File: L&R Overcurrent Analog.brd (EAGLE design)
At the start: 100 x 80 mm, 17 parts, among them IC1 CSLA2CFTH, IC2 TLC393CPN, Q1 SUP75P0307, Q2 SUP75P0307, X1 J1

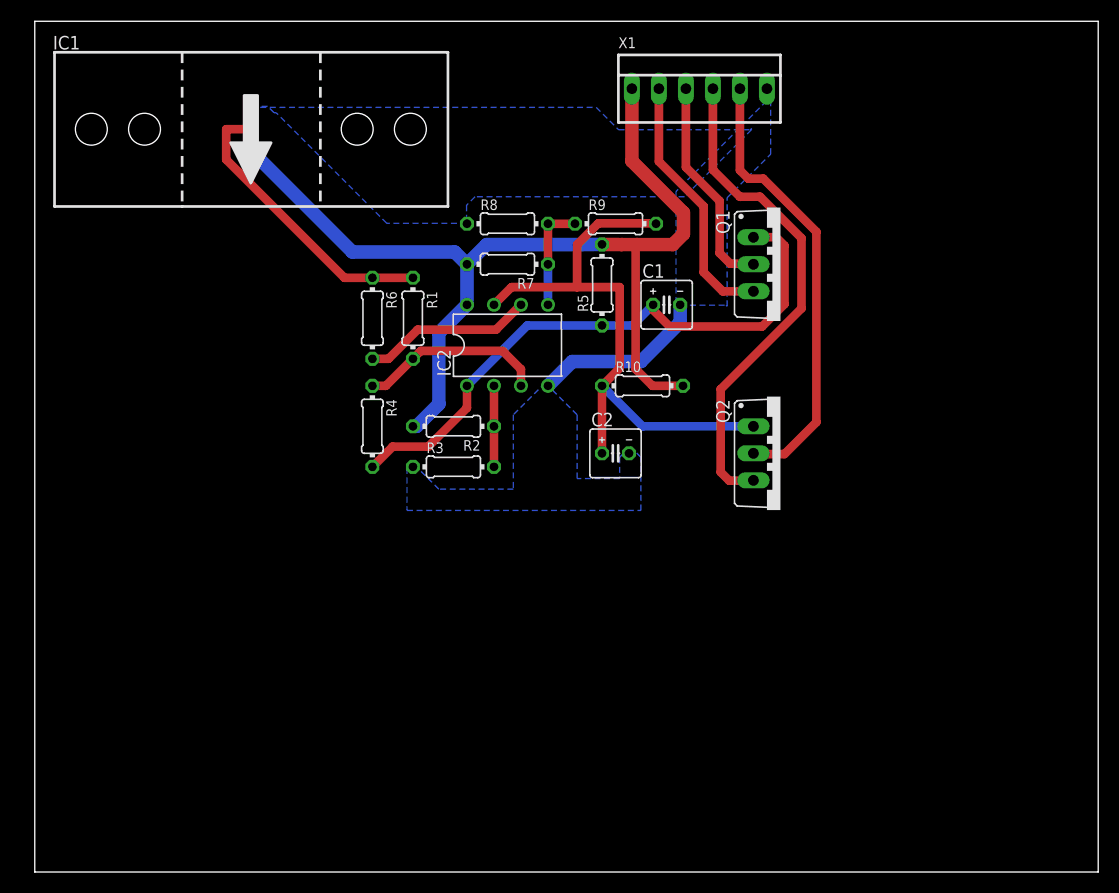
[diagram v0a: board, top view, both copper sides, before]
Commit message: Moved current transducer closer on board, larger ground pour.
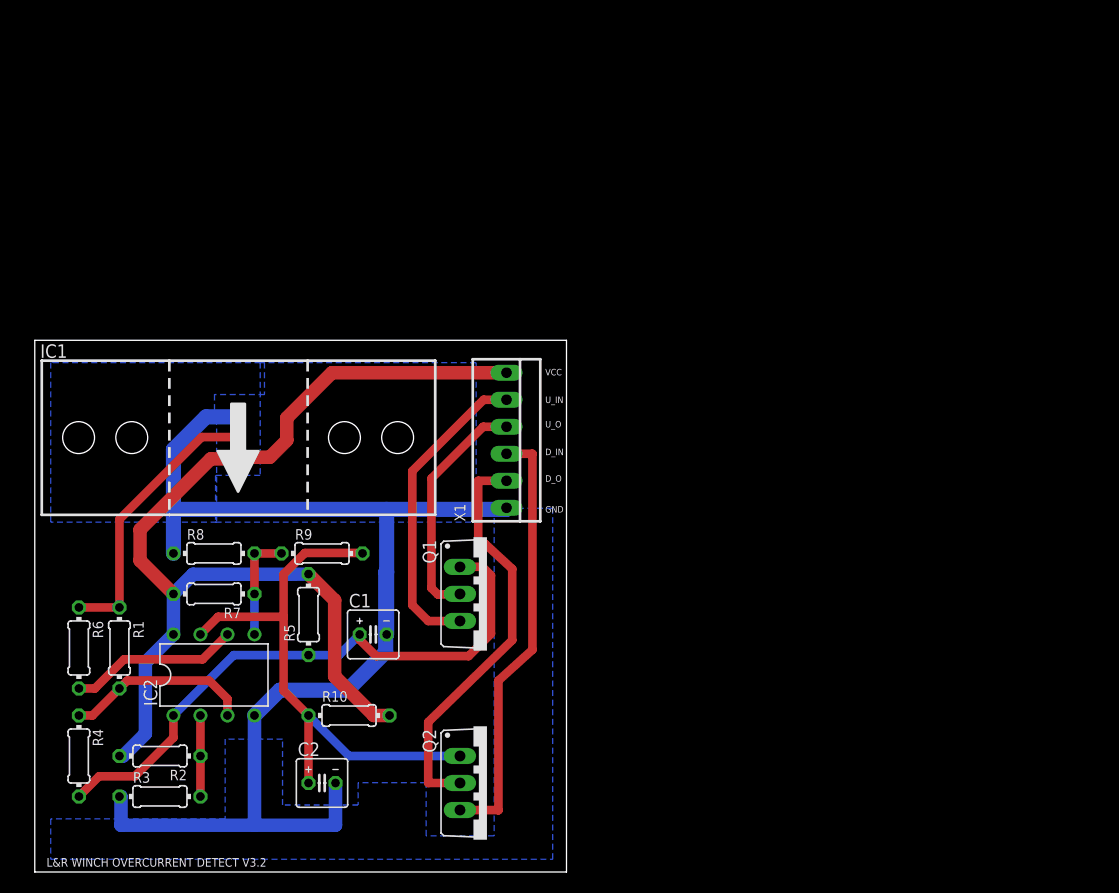
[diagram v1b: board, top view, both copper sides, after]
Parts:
- moved C1 41.5 mm to (31.8, 22.3)
- moved C2 41.5 mm to (27.0, 8.37)
- moved IC2 41.5 mm to (16.9, 18.5)
- moved Q1 41.5 mm to (42.5, 26.1)
- moved Q2 41.5 mm to (42.5, 8.37)
- moved R1 41.5 mm to (7.96, 21.1)
- moved R10 41.5 mm to (29.6, 14.7)
- moved R3 41.5 mm to (11.8, 7.10)
- moved R5 41.5 mm to (25.7, 24.2)
- moved R6 41.5 mm to (4.15, 21.1)
- moved R7 41.5 mm to (16.9, 26.1)
- moved R8 41.5 mm to (16.9, 30.0)
- moved R9 41.5 mm to (27.0, 30.0)
- moved R2 41.5 mm to (11.8, 10.9)
- moved R4 41.5 mm to (4.15, 10.9)
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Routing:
- net GND: track 16.6 -> 120.1 mm
- net N$10: track 47.2 -> 41.0 mm
- net N$8: track 24.4 -> 29.3 mm
- net N$7: track 57.0 -> 53.3 mm
- net N$11: track 42.3 -> 39.1 mm
- net N$9: track 20.4 -> 22.3 mm
- net +12V: track 96.4 -> 97.5 mm
- net N$3: track 27.3 -> 26.5 mm
- removed copper zone on layer 16, net N$12
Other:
- board size 100 x 80 mm -> 50 x 50 mm
- board text added: "D_IN"
- board text added: "D_O"
- board text added: "GND"
- board text added: "L&R WINCH OVERCURRENT DETECT V3.2"
- board text added: "U_IN"
- board text added: "U_O"
- board text added: "VCC"

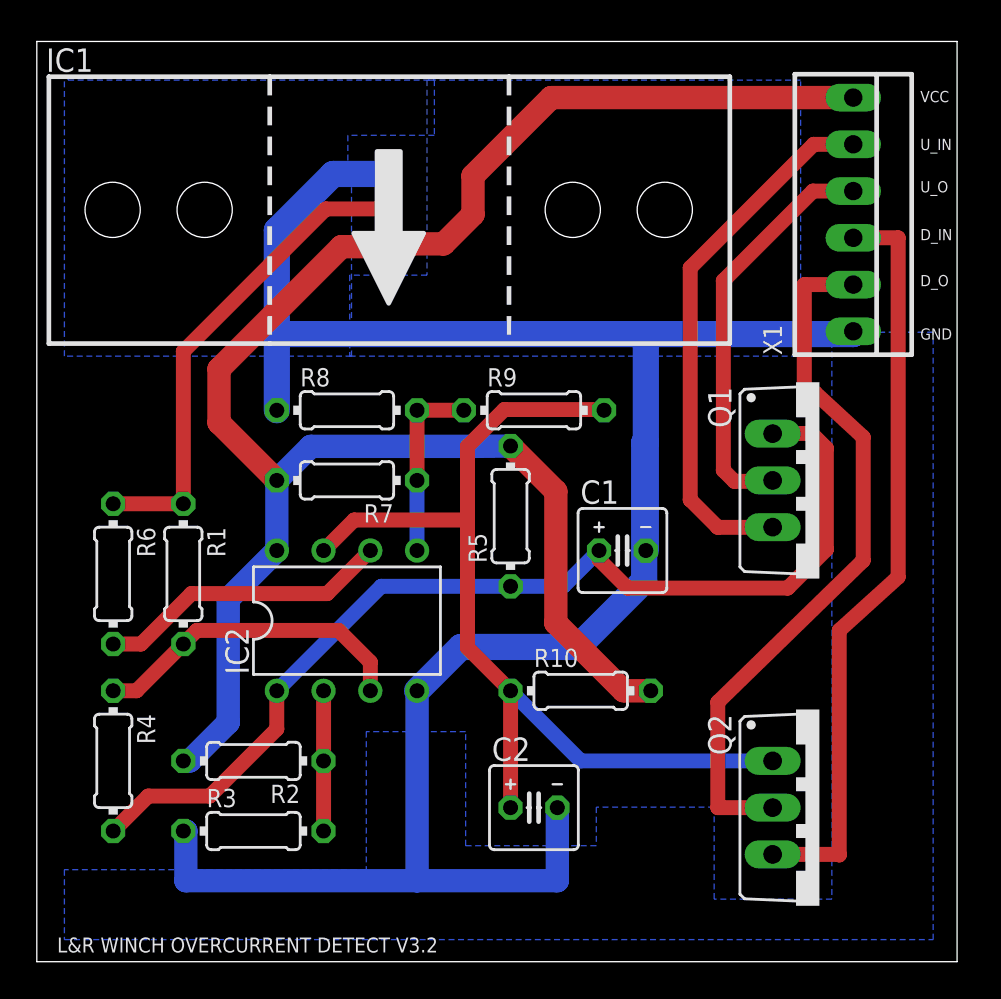
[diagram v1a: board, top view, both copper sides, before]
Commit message: Added IC filter cap, changed RC timer caps to electrolytic.
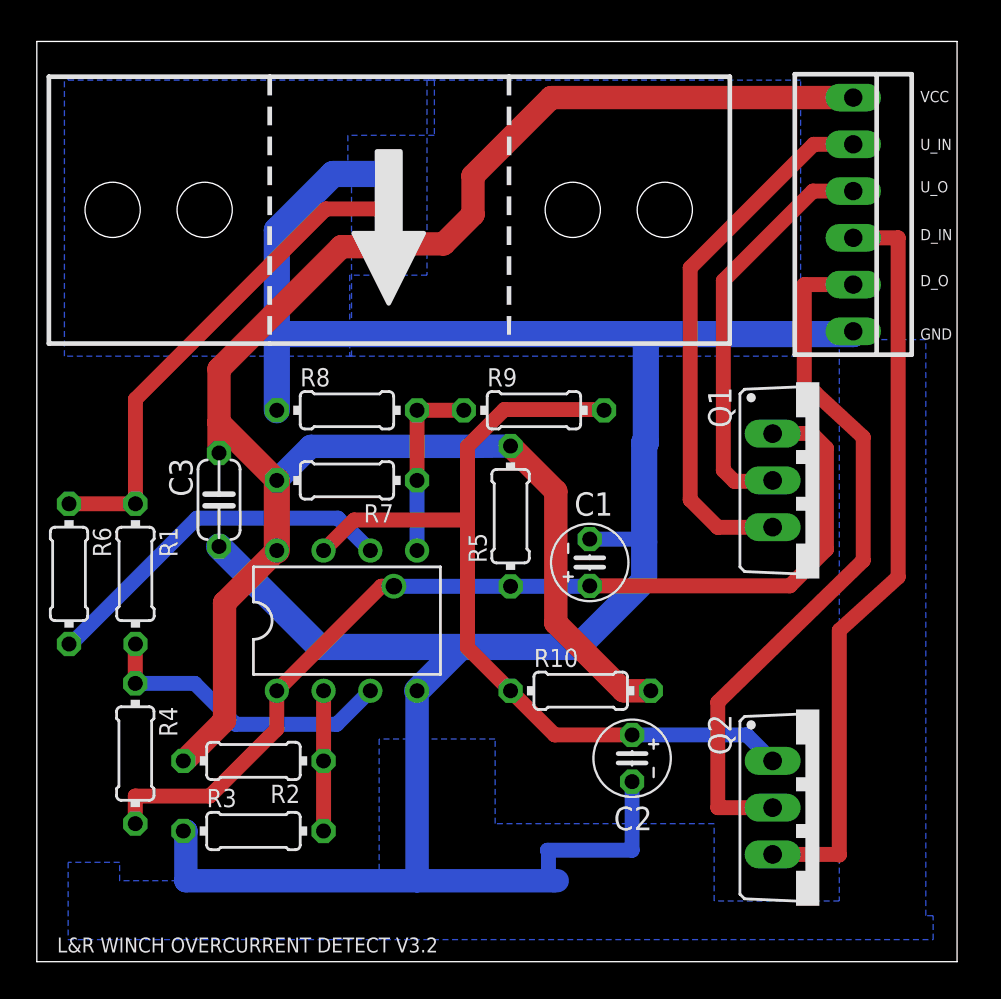
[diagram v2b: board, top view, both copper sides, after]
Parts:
- added C3: 0.1u, Overcurrent Detect:C050-024X044
- moved C2 5.97 mm to (32.3, 11.1), turned to 270 degrees
- moved R1 2.60 mm to (5.36, 21.1)
- moved R6 2.40 mm to (1.75, 21.1)
- moved C1 1.89 mm to (30.0, 21.7), turned to 90 degrees
- moved R4 1.26 mm to (5.35, 11.3)
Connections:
- net +12V: now also C3.1
- net GND: now also C3.2
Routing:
- net GND: track 120.1 -> 138.8 mm
- net N$7: track 53.3 -> 46.9 mm
- net N$4: track 16.1 -> 19.9 mm
- net N$6: track 57.0 -> 54.6 mm, vias 0 -> 1
- net +12V: track 97.5 -> 99.0 mm
- net N$1: track 17.6 -> 16.6 mm
- net N$3: track 26.5 -> 27.4 mm

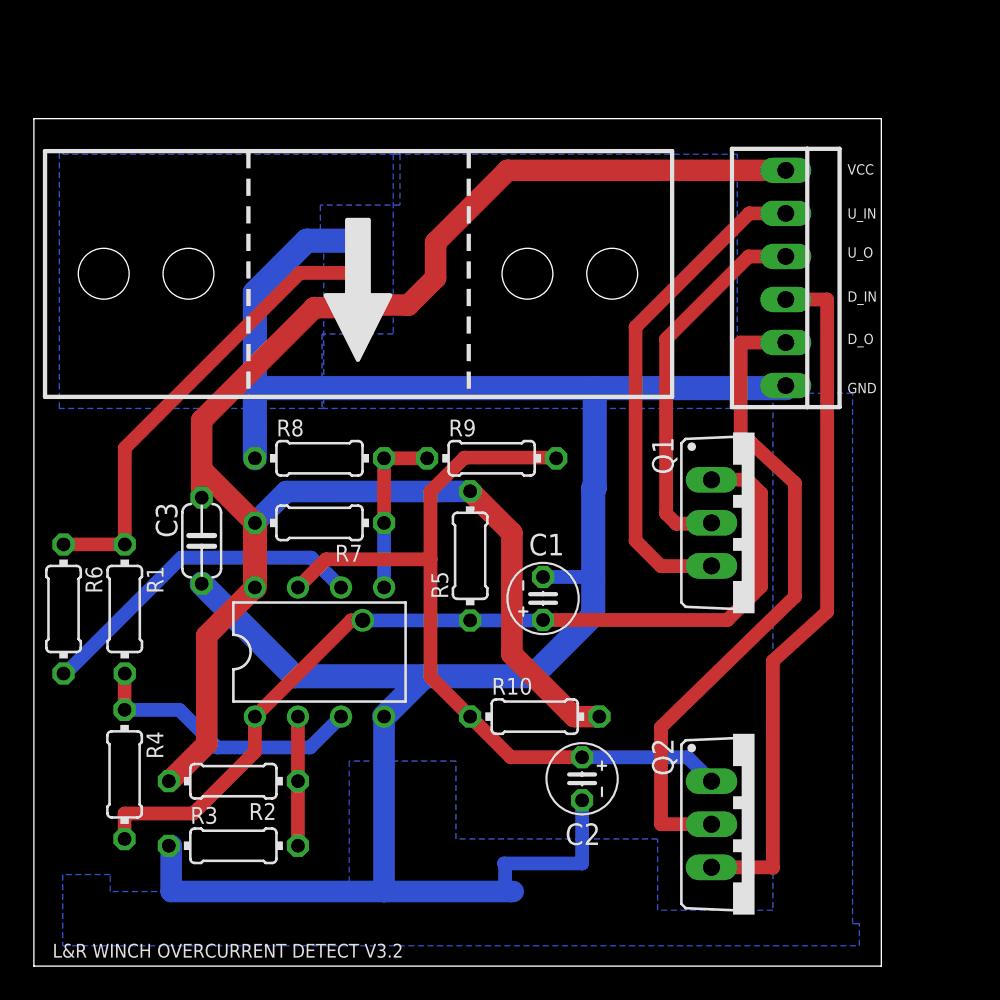
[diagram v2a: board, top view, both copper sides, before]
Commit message: Added stand off holes to board, increased board size.
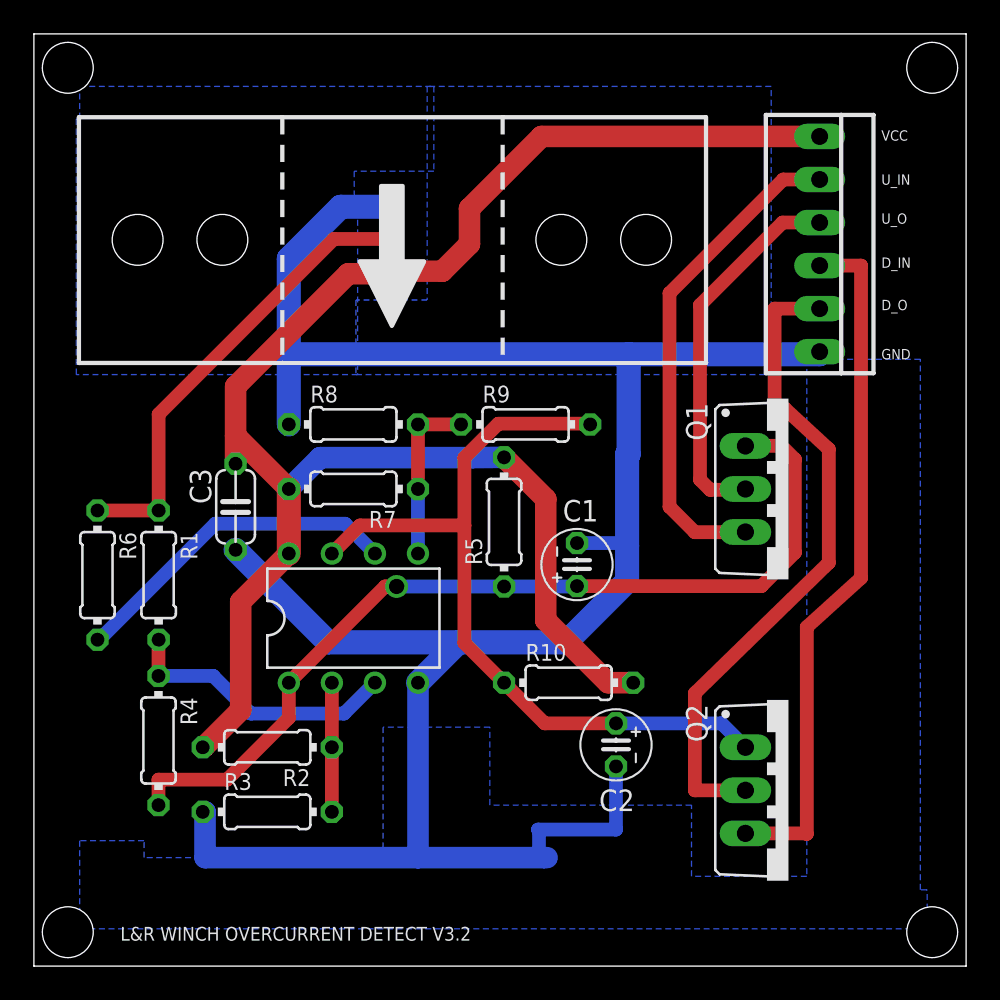
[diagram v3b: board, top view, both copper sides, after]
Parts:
- moved C1 2.83 mm to (32.0, 23.7)
- moved C2 2.83 mm to (34.3, 13.1)
- moved C3 2.83 mm to (11.9, 27.1)
- moved IC1 2.83 mm to (21.1, 42.9)
- moved IC2 2.83 mm to (18.9, 20.5)
- moved Q1 2.83 mm to (44.5, 28.1)
- moved Q2 2.83 mm to (44.5, 10.4)
- moved R1 2.83 mm to (7.36, 23.1)
- moved R2 2.83 mm to (13.8, 12.9)
- moved R3 2.83 mm to (13.8, 9.10)
- moved R4 2.83 mm to (7.35, 13.3)
- moved R5 2.83 mm to (27.7, 26.2)
- moved R6 2.83 mm to (3.75, 23.1)
- moved R7 2.83 mm to (18.9, 28.1)
- moved R8 2.83 mm to (18.9, 32.0)
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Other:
- board size 50 x 50 mm -> 55 x 55 mm

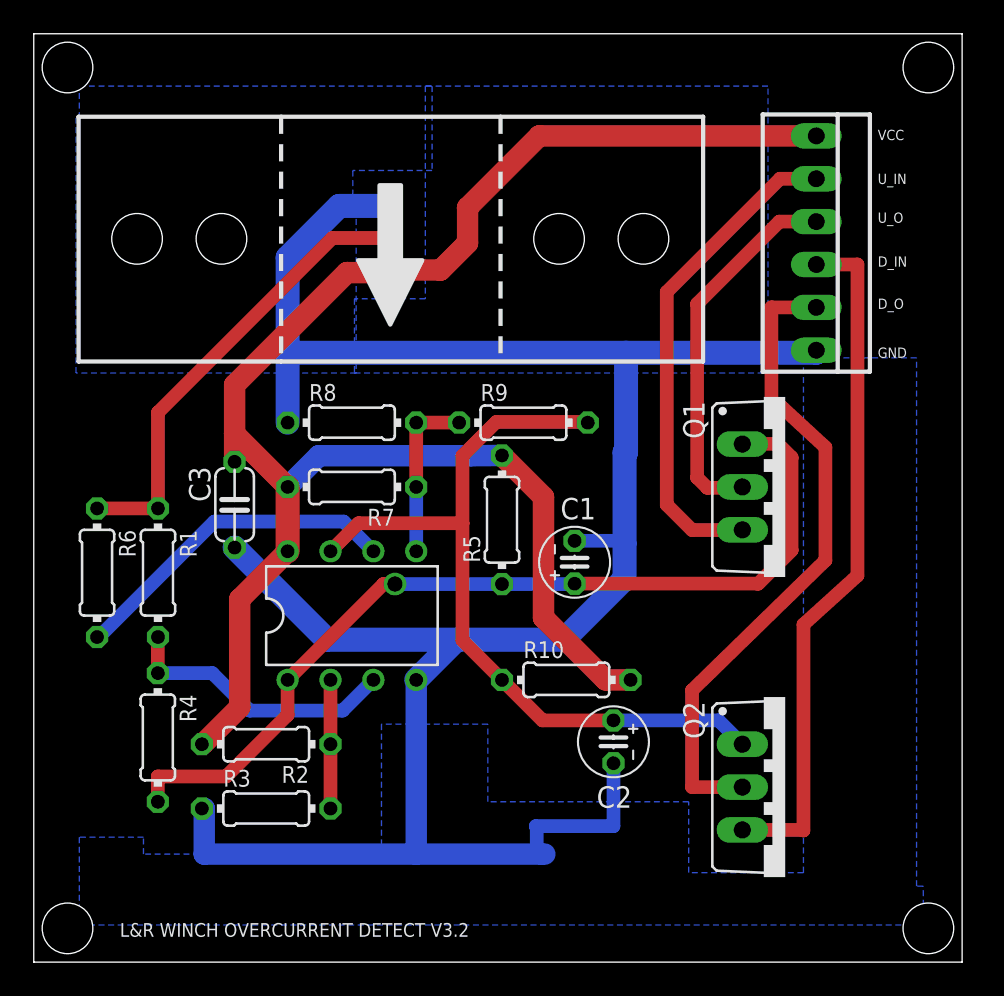
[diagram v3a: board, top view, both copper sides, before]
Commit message: Changed to 5V, added regulator. PCB not done.
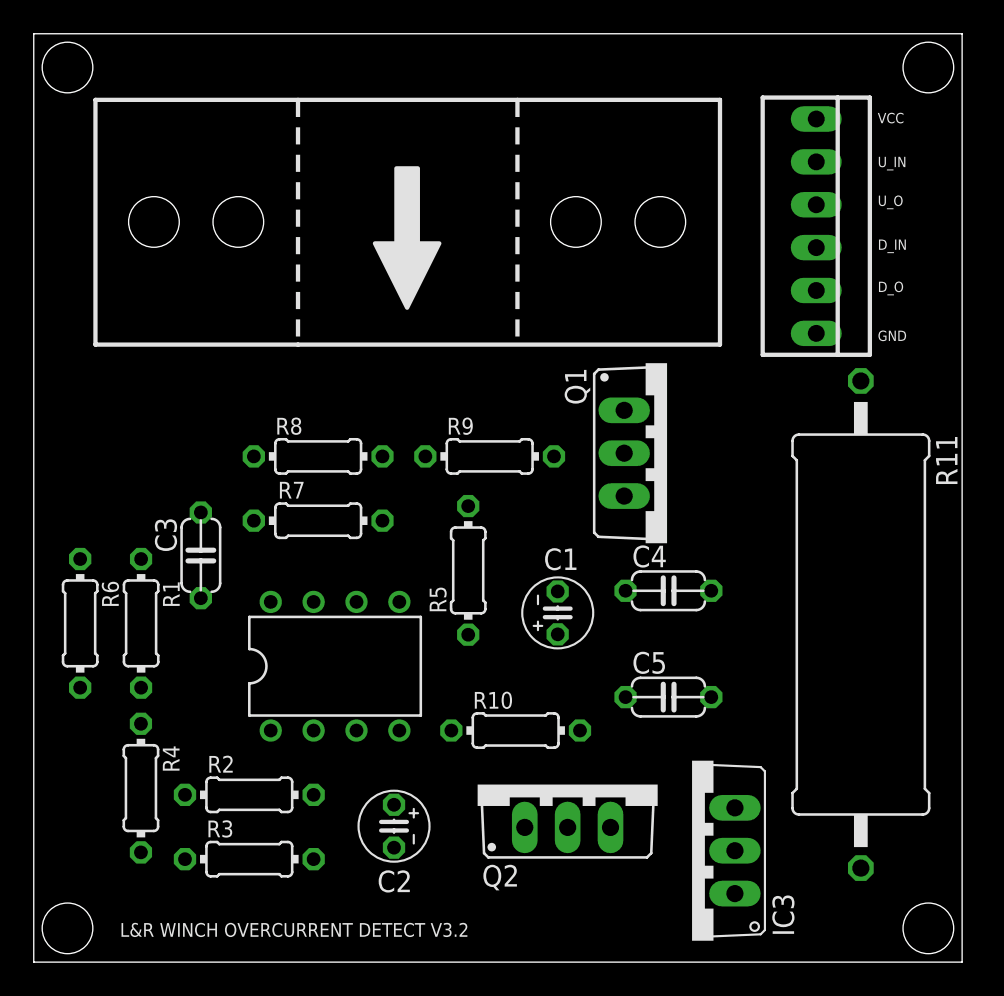
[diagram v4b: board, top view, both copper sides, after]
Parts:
- added C4: 0.33u, Overcurrent Detect:C050-024X044
- added C5: 0.1u, Overcurrent Detect:C050-024X044
- added IC3: 7805TV, Overcurrent Detect:TO220V
- added R11: 2, Overcurrent Detect:0617/22
- moved C2 13.9 mm to (21.3, 8.05)
- moved Q2 12.9 mm to (31.6, 10.5), turned to 0 degrees
- moved Q1 7.28 mm to (37.5, 30.1)
- moved R10 4.24 mm to (28.6, 13.7)
- moved C3 3.61 mm to (9.90, 24.1)
- moved R5 3.61 mm to (25.7, 23.2)
- moved C1 3.16 mm to (31.0, 20.7)
- moved IC2 3.16 mm to (17.9, 17.5)
- moved R1 3.16 mm to (6.36, 20.1)
- moved R2 3.16 mm to (12.8, 9.91)
- moved R3 3.16 mm to (12.8, 6.10)
- moved R4 3.16 mm to (6.35, 10.3)
- moved R6 3.16 mm to (2.75, 20.1)
- moved R7 2.83 mm to (16.9, 26.1)
- moved R8 2.83 mm to (16.9, 30.0)
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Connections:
- new net +5V: C3.1, C5.1, IC1.V+, IC2.8, IC3.3, R10.2, R2.2, R5.2, R7.2
- new net N$12: C4.1, IC3.1, R11.2
- net +12V: now also R11.1; no longer C3.1, IC1.V+, IC2.8, R10.2, R2.2, R5.2, R7.2
- net GND: now also C4.2, C5.2, IC3.2
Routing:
- net GND: track 138.8 -> 0.00 mm
- net +12V: track 99.0 -> 0.00 mm
- net N$6: track 54.6 -> 0.00 mm, vias 1 -> 0
- net N$7: track 46.9 -> 0.00 mm
- net N$10: track 41.0 -> 0.00 mm
- net N$11: track 39.1 -> 0.00 mm
- net N$8: track 29.3 -> 0.00 mm
- net N$3: track 27.4 -> 0.00 mm
- net N$9: track 22.3 -> 0.00 mm
- net N$4: track 19.9 -> 0.00 mm
- net N$1: track 16.6 -> 0.00 mm
- net N$5: track 10.2 -> 0.00 mm
- net N$2: track 7.62 -> 0.00 mm
- removed copper zone on layer 16, net GND
